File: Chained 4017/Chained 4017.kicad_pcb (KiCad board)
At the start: 2 copper layers, 60 parts, among them SW201 SW_Push, U201 LM555xM, U301 4017, U302 4017, U303 4017, U304 74HC00

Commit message: More layout
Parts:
- added D301: LED, LED_THT:LED_D3.0mm, F.Cu at (81.3, 81.3)
- added D302: LED, LED_THT:LED_D3.0mm, F.Cu at (152.4, 81.3)
- added D303: LED, LED_THT:LED_D3.0mm, F.Cu at (223.5, 81.3)
- added D304: LED, LED_THT:LED_D3.0mm, F.Cu at (106.7, 81.3)
- added R301: R, Resistor_THT:R_Axial_DIN0207_L6.3mm_D2.5mm_P7.62mm_Horizontal, F.Cu at (73.7, 23.4)
- added R302: R, Resistor_THT:R_Axial_DIN0207_L6.3mm_D2.5mm_P7.62mm_Horizontal, F.Cu at (73.7, 27.5)
- added R303: R, Resistor_THT:R_Axial_DIN0207_L6.3mm_D2.5mm_P7.62mm_Horizontal, F.Cu at (73.7, 31.5)
- added R304: R, Resistor_THT:R_Axial_DIN0207_L6.3mm_D2.5mm_P7.62mm_Horizontal, F.Cu at (73.7, 35.6)
- moved U302 10.8 mm to (121.9, 66.0)
- moved U301 7.62 mm to (50.8, 66.0)
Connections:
- net Net-(U301-CKEN) renamed /Triple 4017/Q9_{0}
- net Net-(U301-Reset) renamed /Triple 4017/Q9_{2}
- net Net-(U302-CKEN) renamed /Triple 4017/Q9_{1}
- net Net-(U302-Q0) renamed /Triple 4017/Q0_{1}
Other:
- board text added: "CLK"
- board text added: "MR"
- board text added: "Q_{0}"
- board text added: "Q_{1}"
- board text added: "Q_{2}"
- board text added: "Q_{3}"
- board text added: "Q_{4}"
- board text added: "Q_{5}"
- board text added: "Q_{6}"
- board text added: "Q_{7}"
- board text added: "Q_{8}"
- board text added: "Q_{9}"
- board text added: "~{CEN}"

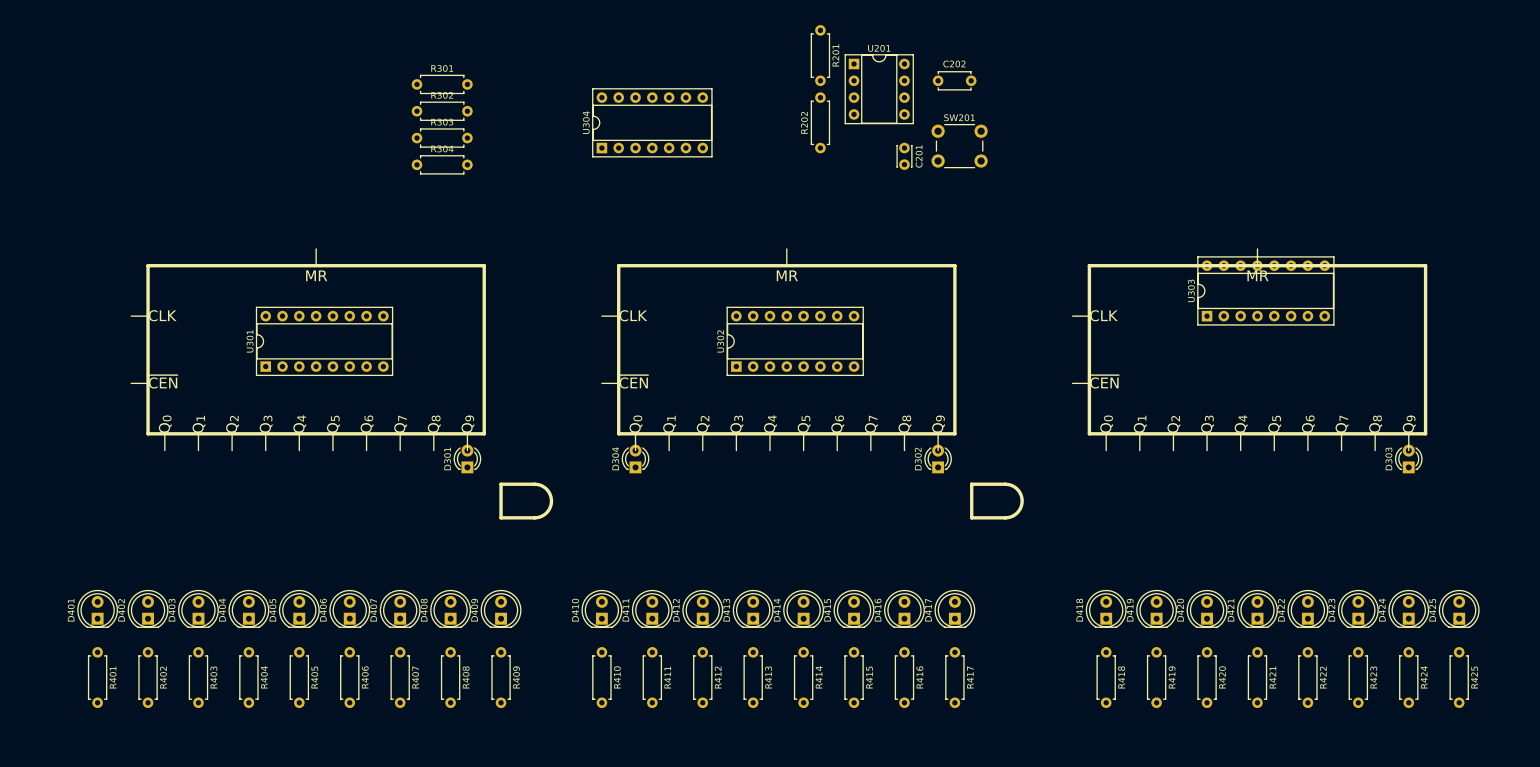
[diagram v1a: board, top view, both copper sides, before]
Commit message: Layout and starting routing
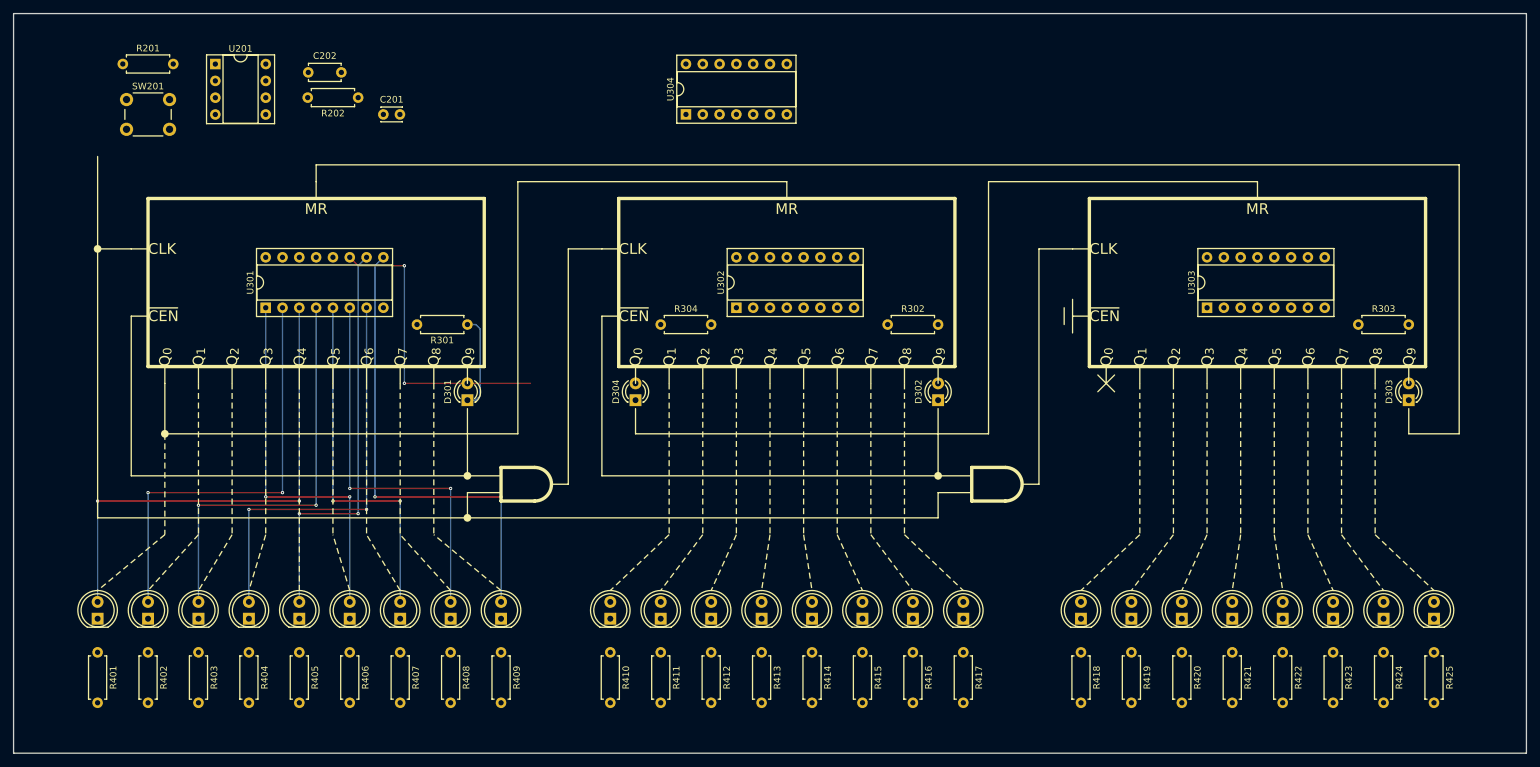
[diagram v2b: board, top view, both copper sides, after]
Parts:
- moved R303 145.0 mm to (215.9, 59.7)
- moved SW201 122.7 mm to (29.8, 25.7)
- moved R201 105.5 mm to (29.2, 20.3), turned to 0 degrees
- moved U201 96.5 mm to (43.2, 20.3)
- moved C202 95.2 mm to (57.2, 21.6)
- moved C201 78.9 mm to (68.6, 27.9), turned to 0 degrees
- moved R302 78.1 mm to (144.8, 59.7)
- moved R202 70.3 mm to (64.8, 25.4), turned to 180 degrees
- moved R304 44.0 mm to (110.5, 59.7)
- moved R301 37.1 mm to (81.3, 59.7), turned to 180 degrees
- moved U304 13.7 mm to (114.3, 27.9)
- moved D301 10.2 mm to (81.3, 71.1)
- moved D302 10.2 mm to (152.4, 71.1)
- moved D303 10.2 mm to (223.5, 71.1)
- moved D304 10.2 mm to (106.7, 71.1)
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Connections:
- D401 pad 2: unconnected-(D401-A-Pad2) -> /Output LEDs/Out0
- D402 pad 2: unconnected-(D402-A-Pad2) -> /Output LEDs/Out1
- D403 pad 2: unconnected-(D403-A-Pad2) -> /Output LEDs/Out2
- D404 pad 2: unconnected-(D404-A-Pad2) -> /Output LEDs/Out3
- D405 pad 2: unconnected-(D405-A-Pad2) -> /Output LEDs/Out4
- D406 pad 2: unconnected-(D406-A-Pad2) -> /Output LEDs/Out5
- D407 pad 2: unconnected-(D407-A-Pad2) -> /Output LEDs/Out6
- D408 pad 2: unconnected-(D408-A-Pad2) -> /Output LEDs/Out7
- D409 pad 2: unconnected-(D409-A-Pad2) -> /Output LEDs/Out8
- D410 pad 2: unconnected-(D410-A-Pad2) -> /Output LEDs/Out9
- D411 pad 2: unconnected-(D411-A-Pad2) -> /Output LEDs/Out10
- D412 pad 2: unconnected-(D412-A-Pad2) -> /Output LEDs/Out11
- D413 pad 2: unconnected-(D413-A-Pad2) -> /Output LEDs/Out12
- D414 pad 2: unconnected-(D414-A-Pad2) -> /Output LEDs/Out13
- D415 pad 2: unconnected-(D415-A-Pad2) -> /Output LEDs/Out14
- D416 pad 2: unconnected-(D416-A-Pad2) -> /Output LEDs/Out15
- R401 pad 2: unconnected-(R401-Pad2) -> GND
- R402 pad 2: unconnected-(R402-Pad2) -> GND
- R403 pad 2: unconnected-(R403-Pad2) -> GND
- R404 pad 2: unconnected-(R404-Pad2) -> GND
- R405 pad 2: unconnected-(R405-Pad2) -> GND
- R406 pad 2: unconnected-(R406-Pad2) -> GND
- R407 pad 2: unconnected-(R407-Pad2) -> GND
- R408 pad 2: unconnected-(R408-Pad2) -> GND
- R409 pad 2: unconnected-(R409-Pad2) -> GND
- R410 pad 2: unconnected-(R410-Pad2) -> GND
- R411 pad 2: unconnected-(R411-Pad2) -> GND
- R412 pad 2: unconnected-(R412-Pad2) -> GND
- R413 pad 2: unconnected-(R413-Pad2) -> GND
- R414 pad 2: unconnected-(R414-Pad2) -> GND
- R415 pad 2: unconnected-(R415-Pad2) -> GND
- R416 pad 2: unconnected-(R416-Pad2) -> GND
- U301 pad 10: /Output LEDs/Out5 -> /Output LEDs/Out4
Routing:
- net /Output LEDs/Out0: track 0.00 -> 74.9 mm, vias 0 -> 2
- net /Output LEDs/Out8: track 0.00 -> 71.6 mm, vias 0 -> 2
- net /Output LEDs/Out1: track 0.00 -> 64.8 mm, vias 0 -> 2
- net /Output LEDs/Out3: track 0.00 -> 62.2 mm, vias 0 -> 2
- net /Output LEDs/Out2: track 0.00 -> 62.2 mm, vias 0 -> 2
- net /Output LEDs/Out4: track 0.00 -> 61.5 mm, vias 0 -> 2
- net /Output LEDs/Out7: track 0.00 -> 59.7 mm, vias 0 -> 2
- net /Output LEDs/Out5: track 0.00 -> 57.1 mm, vias 0 -> 2
- net /Output LEDs/Out6: track 0.00 -> 54.6 mm, vias 0 -> 2
- net /Triple 4017/Q9_{0}: track 0.00 -> 45.6 mm, vias 0 -> 2
- net Net-(D301-K): track 0.00 -> 14.5 mm
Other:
- board outline added: 228.6 x 111.8 mm

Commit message: Capacitors and routing
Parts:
- added C301: 0.1u, Capacitor_THT:C_Disc_D4.3mm_W1.9mm_P5.00mm, F.Cu at (47.0, 55.9)
- added C302: 0.1u, Capacitor_THT:C_Disc_D4.3mm_W1.9mm_P5.00mm, F.Cu at (118.1, 55.9)
- added C303: 0.1u, Capacitor_THT:C_Disc_D4.3mm_W1.9mm_P5.00mm, F.Cu at (189.2, 55.9)
- added C304: 0.1u, Capacitor_THT:C_Disc_D4.3mm_W1.9mm_P5.00mm, F.Cu at (110.5, 26.6)
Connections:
- D417 pad 2: unconnected-(D417-A-Pad2) -> /Output LEDs/Out16
- D418 pad 2: unconnected-(D418-A-Pad2) -> /Output LEDs/Out17
- D419 pad 2: unconnected-(D419-A-Pad2) -> /Output LEDs/Out18
- D420 pad 2: unconnected-(D420-A-Pad2) -> /Output LEDs/Out19
- D421 pad 2: unconnected-(D421-A-Pad2) -> /Output LEDs/Out20
- D422 pad 2: unconnected-(D422-A-Pad2) -> /Output LEDs/Out21
- D423 pad 2: unconnected-(D423-A-Pad2) -> /Output LEDs/Out22
- D424 pad 2: unconnected-(D424-A-Pad2) -> /Output LEDs/Out23
- D425 pad 2: unconnected-(D425-A-Pad2) -> /Output LEDs/Out24
- R417 pad 2: unconnected-(R417-Pad2) -> GND
- R418 pad 2: unconnected-(R418-Pad2) -> GND
- R419 pad 2: unconnected-(R419-Pad2) -> GND
- R420 pad 2: unconnected-(R420-Pad2) -> GND
- R421 pad 2: unconnected-(R421-Pad2) -> GND
- R422 pad 2: unconnected-(R422-Pad2) -> GND
- R423 pad 2: unconnected-(R423-Pad2) -> GND
- R424 pad 2: unconnected-(R424-Pad2) -> GND
- R425 pad 2: unconnected-(R425-Pad2) -> GND
- U304 pad 10: /Clock Signal/CLOCK -> Net-(U304-Pad10)
- U304 pad 11: Net-(U303-CLK) -> Net-(U302-CLK)
- U304 pad 3: Net-(U304-Pad3) -> Net-(U304-Pad12)
- U304 pad 4: Net-(U304-Pad3) -> /Triple 4017/Q9_{1}
- U304 pad 5: Net-(U304-Pad3) -> /Clock Signal/CLOCK
- U304 pad 6: Net-(U302-CLK) -> Net-(U304-Pad10)
- U304 pad 8: Net-(U304-Pad12) -> Net-(U303-CLK)
- U304 pad 9: /Triple 4017/Q9_{1} -> Net-(U304-Pad10)
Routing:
- net /Triple 4017/Q9_{2}: track 0.00 -> 227.6 mm, vias 0 -> 3
- net /Triple 4017/Q0_{1}: track 0.00 -> 117.7 mm, vias 0 -> 4
- net Net-(U303-CLK): track 0.00 -> 97.8 mm, vias 0 -> 1
- net /Clock Signal/CLOCK: track 0.00 -> 94.1 mm, vias 0 -> 1
- net /Triple 4017/Q9_{1}: track 0.00 -> 82.3 mm, vias 0 -> 3
- net /Output LEDs/Out0: track 74.9 -> 155.5 mm, vias 2 -> 4
- net /Output LEDs/Out24: track 0.00 -> 70.4 mm, vias 0 -> 2
- net /Output LEDs/Out16: track 0.00 -> 70.4 mm, vias 0 -> 2
- net /Output LEDs/Out9: track 0.00 -> 66.0 mm, vias 0 -> 2
- net /Output LEDs/Out17: track 0.00 -> 66.0 mm, vias 0 -> 2
- net /Triple 4017/Q9_{0}: track 45.6 -> 109.4 mm, vias 2 -> 4
- net /Output LEDs/Out19: track 0.00 -> 63.5 mm, vias 0 -> 2
- net /Output LEDs/Out11: track 0.00 -> 63.5 mm, vias 0 -> 2
- net /Output LEDs/Out10: track 0.00 -> 63.5 mm, vias 0 -> 2
- net /Output LEDs/Out18: track 0.00 -> 63.5 mm, vias 0 -> 2
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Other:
- board text added: "RGE2023"

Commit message: Complete routing
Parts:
- added H101: MountingHole, MountingHole:MountingHole_2.7mm_M2.5_ISO7380, F.Cu at (20.3, 20.3)
- added H102: MountingHole, MountingHole:MountingHole_2.7mm_M2.5_ISO7380, F.Cu at (233.7, 20.3)
- added H103: MountingHole, MountingHole:MountingHole_2.7mm_M2.5_ISO7380, F.Cu at (233.7, 116.8)
- added H104: MountingHole, MountingHole:MountingHole_2.7mm_M2.5_ISO7380, F.Cu at (20.3, 116.8)
- added J101: USB_A, Connector_USB:USB_A_Molex_67643_Horizontal, F.Cu at (213.4, 25.7)
- added J102: Conn_01x02_Pin, Connector_PinHeader_2.54mm:PinHeader_1x02_P2.54mm_Vertical, F.Cu at (223.5, 25.4)
- moved R201 20.8 mm to (45.7, 33.0)
- moved C202 10.9 mm to (63.5, 30.5)
- moved U201 10.8 mm to (50.8, 27.9), turned to 90 degrees
- moved C201 9.14 mm to (63.5, 20.3)
- moved SW201 2.90 mm to (31.6, 27.9)
- moved R202 1.27 mm to (63.5, 25.4), turned to 0 degrees
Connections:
- R202 pad 1: +5V -> Net-(U201-DIS)
- R202 pad 2: Net-(U201-DIS) -> +5V
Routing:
- net Net-(U201-TR): track 0.00 -> 31.2 mm
- net Net-(U201-DIS): track 0.00 -> 19.9 mm
- net unconnected-(J101-Shield-Pad5): track 0.00 -> 13.1 mm
- net /Clock Signal/CLOCK: track 94.1 -> 104.3 mm
- net /Triple 4017/Q9_{0}: track 109.4 -> 118.4 mm, vias 4 -> 6
- net Net-(U201-CV): track 0.00 -> 5.12 mm
- net Net-(J101-D+): track 0.00 -> 2.00 mm
- added copper zone on B.Cu, net +5V
- added copper zone on F.Cu, net GND
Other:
- board text added: "+5V"
- board text added: "Chained 4017"
- board text added: "Clock"
- board text added: "GND"
